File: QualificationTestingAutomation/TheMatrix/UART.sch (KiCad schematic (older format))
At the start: 23 parts, among them Q3 2N7002DW, Q4 2N7002DW, Q5 2N7002DW, Q6 2N7002DW, U20 CD4070B, U32 MAX324CUA

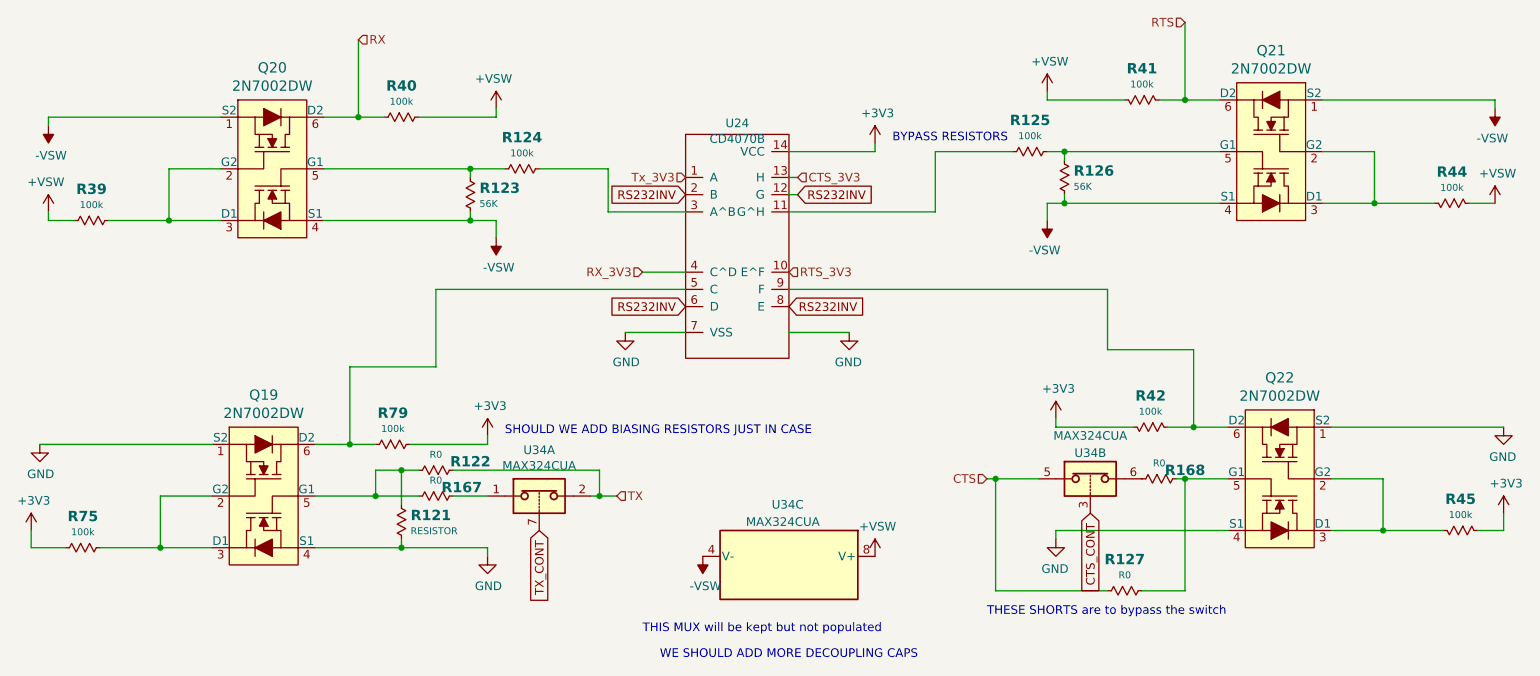
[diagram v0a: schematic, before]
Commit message: Added 60V supply for the MUX's so they can be independent from Vpower, Added another seperate power rail
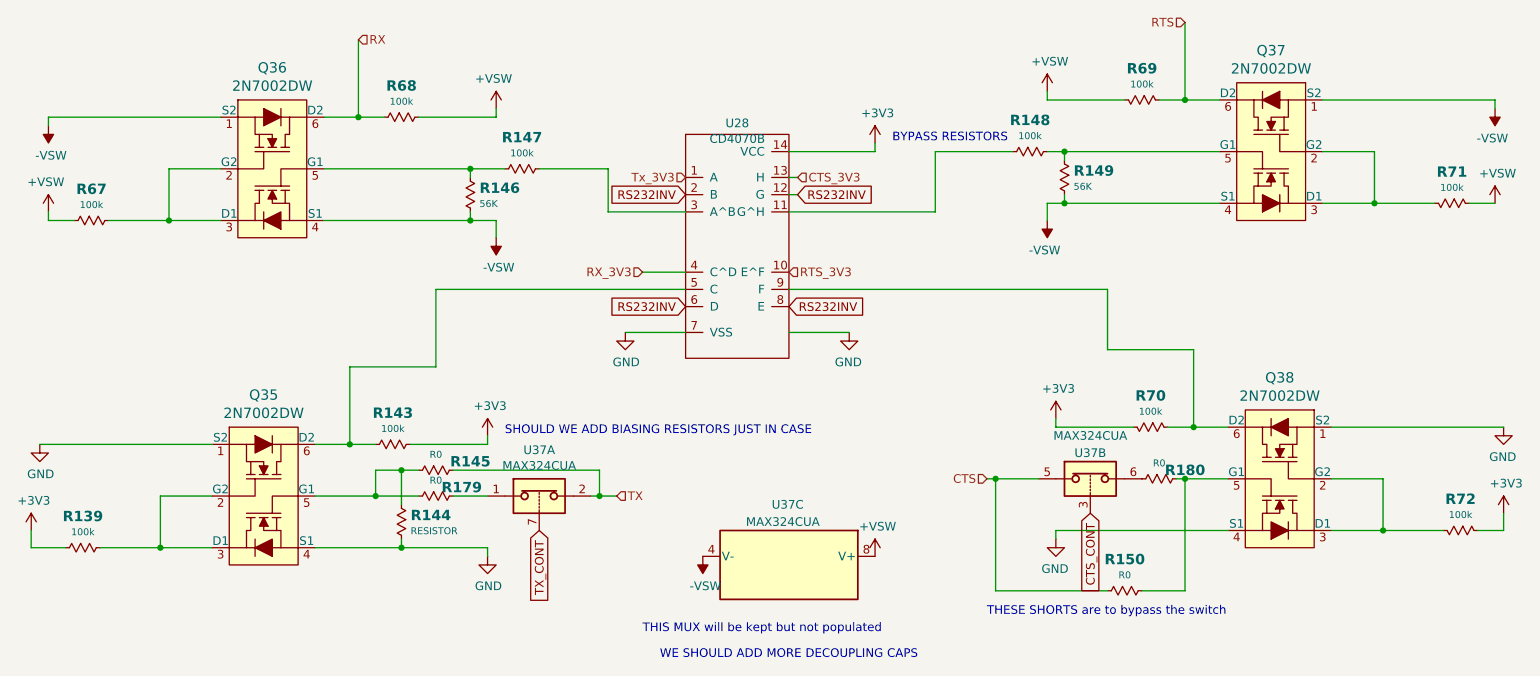
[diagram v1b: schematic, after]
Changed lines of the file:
@@
 AR Path="/5BB9E3C7/5BDC515F/5C46C762" Ref="Q35"  Part="1"
 AR Path="/5BB9E3C7/5BDC5169/5C46C762" Ref="Q39"  Part="1"
-F 0 "Q19" H 3450 4987 60  0000 C CNN
+F 0 "Q35" H 3450 4987 60  0000 C CNN
 F 1 "2N7002DW" H 3450 4881 60  0000 C CNN
 F 2 "digikey-footprints:SOT-363" H 3650 4700 60  0001 L CNN
@@
 AR Path="/5BB9E3C7/5BDC515F/5C46C76E" Ref="R143"  Part="1"
 AR Path="/5BB9E3C7/5BDC5169/5C46C76E" Ref="R159"  Part="1"
-F 0 "R79" H 4200 4482 60  0000 C CNB
+F 0 "R143" H 4200 4482 60  0000 C CNB
 F 1 "100k" H 4200 4391 40  0000 C CNN
 F 2 "Resistor_SMD:R_0402_1005Metric" H 4200 4160 40  0001 C CNN
@@
 AR Path="/5BB9E3C7/5BDC515F/5C46C789" Ref="R139"  Part="1"
 AR Path="/5BB9E3C7/5BDC5169/5C46C789" Ref="R155"  Part="1"
-F 0 "R75" H 2400 5082 60  0000 C CNB
+F 0 "R139" H 2400 5082 60  0000 C CNB
 F 1 "100k" H 2400 4991 40  0000 C CNN
 F 2 "Resistor_SMD:R_0402_1005Metric" H 2400 4760 40  0001 C CNN
@@
 AR Path="/5BB9E3C7/5BDC515F/5BC01C7A" Ref="Q36"  Part="1"
 AR Path="/5BB9E3C7/5BDC5169/5BC01C7A" Ref="Q40"  Part="1"
-F 0 "Q20" H 3500 3087 60  0000 C CNN
+F 0 "Q36" H 3500 3087 60  0000 C CNN
 F 1 "2N7002DW" H 3500 2981 60  0000 C CNN
 F 2 "digikey-footprints:SOT-363" H 3700 2800 60  0001 L CNN
@@
 AR Path="/5BB9E3C7/5BDC515F/5BC01C85" Ref="R68"  Part="1"
 AR Path="/5BB9E3C7/5BDC5169/5BC01C85" Ref="R74"  Part="1"
-F 0 "R40" H 4250 2582 60  0000 C CNB
+F 0 "R68" H 4250 2582 60  0000 C CNB
 F 1 "100k" H 4250 2491 40  0000 C CNN
 F 2 "Resistor_SMD:R_0402_1005Metric" H 4250 2260 40  0001 C CNN
@@
 AR Path="/5BB9E3C7/5BDC515F/5BC01C95" Ref="R67"  Part="1"
 AR Path="/5BB9E3C7/5BDC5169/5BC01C95" Ref="R73"  Part="1"
-F 0 "R39" H 2450 3182 60  0000 C CNB
+F 0 "R67" H 2450 3182 60  0000 C CNB
 F 1 "100k" H 2450 3091 40  0000 C CNN
 F 2 "Resistor_SMD:R_0402_1005Metric" H 2450 2860 40  0001 C CNN
@@
 AR Path="/5BB9E3C7/5BDC515F/5BC141FA" Ref="Q38"  Part="1"
 AR Path="/5BB9E3C7/5BDC5169/5BC141FA" Ref="Q42"  Part="1"
-F 0 "Q22" H 9350 4887 60  0000 C CNN
+F 0 "Q38" H 9350 4887 60  0000 C CNN
 F 1 "2N7002DW" H 9350 4781 60  0000 C CNN
 F 2 "digikey-footprints:SOT-363" H 9550 4600 60  0001 L CNN
@@
 AR Path="/5BB9E3C7/5BDC515F/5BC14205" Ref="R70"  Part="1"
 AR Path="/5BB9E3C7/5BDC5169/5BC14205" Ref="R77"  Part="1"
-F 0 "R42" H 8600 4382 60  0000 C CNB
+F 0 "R70" H 8600 4382 60  0000 C CNB
 F 1 "100k" H 8600 4291 40  0000 C CNN
 F 2 "Resistor_SMD:R_0402_1005Metric" H 8600 4060 40  0001 C CNN
@@
 AR Path="/5BB9E3C7/5BDC515F/5BC14215" Ref="R72"  Part="1"
 AR Path="/5BB9E3C7/5BDC5169/5BC14215" Ref="R80"  Part="1"
-F 0 "R45" H 10400 4982 60  0000 C CNB
+F 0 "R72" H 10400 4982 60  0000 C CNB
 F 1 "100k" H 10400 4891 40  0000 C CNN
 F 2 "Resistor_SMD:R_0402_1005Metric" H 10400 4660 40  0001 C CNN
@@
 AR Path="/5BB9E3C7/5BDC515F/5BC14248" Ref="Q37"  Part="1"
 AR Path="/5BB9E3C7/5BDC5169/5BC14248" Ref="Q41"  Part="1"
-F 0 "Q21" H 9300 2987 60  0000 C CNN
+F 0 "Q37" H 9300 2987 60  0000 C CNN
 F 1 "2N7002DW" H 9300 2881 60  0000 C CNN
 F 2 "digikey-footprints:SOT-363" H 9500 2700 60  0001 L CNN
@@
 AR Path="/5BB9E3C7/5BDC515F/5BC14252" Ref="R69"  Part="1"
 AR Path="/5BB9E3C7/5BDC5169/5BC14252" Ref="R76"  Part="1"
-F 0 "R41" H 8550 2482 60  0000 C CNB
+F 0 "R69" H 8550 2482 60  0000 C CNB
 F 1 "100k" H 8550 2391 40  0000 C CNN
 F 2 "Resistor_SMD:R_0402_1005Metric" H 8550 2160 40  0001 C CNN
@@
 AR Path="/5BB9E3C7/5BDC515F/5BC14262" Ref="R71"  Part="1"
 AR Path="/5BB9E3C7/5BDC5169/5BC14262" Ref="R78"  Part="1"
-F 0 "R44" H 10350 3082 60  0000 C CNB
+F 0 "R71" H 10350 3082 60  0000 C CNB
 F 1 "100k" H 10350 2991 40  0000 C CNN
 F 2 "Resistor_SMD:R_0402_1005Metric" H 10350 2760 40  0001 C CNN
@@
 AR Path="/5BB9E3C7/5BD54793/5BD62A8F" Ref="U36"  Part="1"
 AR Path="/5BB9E3C7/5BDC515F/5BD62A8F" Ref="U37"  Part="1"
-F 0 "U34" H 5050 4867 50  0000 C CNN
+F 0 "U37" H 5050 4867 50  0000 C CNN
 F 1 "MAX324CUA" H 5050 4776 50  0000 C CNN
 F 2 "Housings_SSOP:MSOP-8_3x3mm_Pitch0.65mm" H 5050 4500 50  0001 C CNN
@@
 AR Path="/5BB9E3C7/5BD54793/5BD6777D" Ref="U36"  Part="2"
 AR Path="/5BB9E3C7/5BDC515F/5BD6777D" Ref="U37"  Part="2"
-F 0 "U34" H 8250 4650 50  0000 C CNN
+F 0 "U37" H 8250 4650 50  0000 C CNN
 F 1 "MAX324CUA" H 8250 4750 50  0000 C CNN
 F 2 "Housings_SSOP:MSOP-8_3x3mm_Pitch0.65mm" H 8250 4400 50  0001 C CNN
@@
 AR Path="/5BB9E3C7/5BD54793/5BD79DC1" Ref="U36"  Part="3"
 AR Path="/5BB9E3C7/5BDC515F/5BD79DC1" Ref="U37"  Part="3"
-F 0 "U34" V 6200 4850 50  0000 L CNN
+F 0 "U37" V 6200 4850 50  0000 L CNN
 F 1 "MAX324CUA" V 6300 4700 50  0000 L CNN
 F 2 "Housings_SSOP:MSOP-8_3x3mm_Pitch0.65mm" H 6500 4850 50  0001 C CNN
@@
 AR Path="/5BB9E3C7/5BD54793/5BBE173B" Ref="R136"  Part="1"
 AR Path="/5BB9E3C7/5BDC515F/5BBE173B" Ref="R145"  Part="1"
-F 0 "R122" H 4650 4500 60  0000 C CNB
+F 0 "R145" H 4650 4500 60  0000 C CNB
 F 1 "R0" H 4450 4541 40  0000 C CNN
 F 2 "Resistor_SMD:R_0402_1005Metric" H 4450 4310 40  0001 C CNN
@@
 AR Path="/5BB9E3C7/5BD54793/5BBEA4F3" Ref="R142"  Part="1"
 AR Path="/5BB9E3C7/5BDC515F/5BBEA4F3" Ref="R150"  Part="1"
-F 0 "R127" H 8450 5332 60  0000 C CNB
+F 0 "R150" H 8450 5332 60  0000 C CNB
 F 1 "R0" H 8450 5241 40  0000 C CNN
 F 2 "Resistor_SMD:R_0402_1005Metric" H 8450 5010 40  0001 C CNN
@@
 AR Path="/5BB9E3C7/5BDC515F/5BBECE3B" Ref="R147"  Part="1"
 AR Path="/5BB9E3C7/5BDC5169/5BBECE3B" Ref="R?"  Part="1"
-F 0 "R124" H 4950 2882 60  0000 C CNB
+F 0 "R147" H 4950 2882 60  0000 C CNB
 F 1 "100k" H 4950 2791 40  0000 C CNN
 F 2 "Resistor_SMD:R_0402_1005Metric" H 4950 2560 40  0001 C CNN
@@
 AR Path="/5BB9E3C7/5BD54793/5BBF422E" Ref="R137"  Part="1"
 AR Path="/5BB9E3C7/5BDC515F/5BBF422E" Ref="R146"  Part="1"
-F 0 "R123" V 4612 2903 60  0000 L CNB
+F 0 "R146" V 4612 2903 60  0000 L CNB
 F 1 "56K" V 4703 2903 40  0000 L CNN
 F 2 "Resistor_SMD:R_0402_1005Metric" H 4650 2710 40  0001 C CNN
@@
 AR Path="/5BB9E3C7/5BDC515F/5BBF9882" Ref="R148"  Part="1"
 AR Path="/5BB9E3C7/5BDC5169/5BBF9882" Ref="R?"  Part="1"
-F 0 "R125" H 7900 2782 60  0000 C CNB
+F 0 "R148" H 7900 2782 60  0000 C CNB
 F 1 "100k" H 7900 2691 40  0000 C CNN
 F 2 "Resistor_SMD:R_0402_1005Metric" H 7900 2460 40  0001 C CNN
@@
 AR Path="/5BB9E3C7/5BD54793/5BC047FB" Ref="R141"  Part="1"
 AR Path="/5BB9E3C7/5BDC515F/5BC047FB" Ref="R149"  Part="1"
-F 0 "R126" V 8062 2803 60  0000 L CNB
+F 0 "R149" V 8062 2803 60  0000 L CNB
 F 1 "56K" V 8153 2803 40  0000 L CNN
 F 2 "Resistor_SMD:R_0402_1005Metric" H 8100 2610 40  0001 C CNN
@@
 AR Path="/5BB9E3C7/5BD54793/5BC0A9BF" Ref="R135"  Part="1"
 AR Path="/5BB9E3C7/5BDC515F/5BC0A9BF" Ref="R144"  Part="1"
-F 0 "R121" V 4212 4803 60  0000 L CNB
+F 0 "R144" V 4212 4803 60  0000 L CNB
 F 1 "RESISTOR" V 4303 4803 40  0000 L CNN
 F 2 "Resistor_SMD:R_0402_1005Metric" H 4250 4610 40  0001 C CNN
@@
 AR Path="/5BB9E3C7/5BDC5169/5C46C7B8" Ref="U29"  Part="1"
 AR Path="/5C46C7B8" Ref="U24"  Part="1"
-F 0 "U24" H 6200 2365 50  0000 C CNN
+F 0 "U28" H 6200 2365 50  0000 C CNN
 F 1 "CD4070B" H 6200 2274 50  0000 C CNN
 F 2 "digikey-footprints:SOIC-14_W3.9mm" H 6150 2350 50  0001 C CNN
@@
 AR Path="/5BB9E3C7/5BD54793/5CACEC46" Ref="R177"  Part="1"
 AR Path="/5BB9E3C7/5BDC515F/5CACEC46" Ref="R179"  Part="1"
-F 0 "R167" H 4600 4650 60  0000 C CNB
+F 0 "R179" H 4600 4650 60  0000 C CNB
 F 1 "R0" H 4450 4691 40  0000 C CNN
 F 2 "Resistor_SMD:R_0402_1005Metric" H 4450 4460 40  0001 C CNN
@@
 AR Path="/5BB9E3C7/5BD54793/5CAD91E6" Ref="R178"  Part="1"
 AR Path="/5BB9E3C7/5BDC515F/5CAD91E6" Ref="R180"  Part="1"
-F 0 "R168" H 8800 4550 60  0000 C CNB
+F 0 "R180" H 8800 4550 60  0000 C CNB
 F 1 "R0" H 8650 4591 40  0000 C CNN
 F 2 "Resistor_SMD:R_0402_1005Metric" H 8650 4360 40  0001 C CNN

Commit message: Major upgrade, Finished laying out switcheroo, and the Matrix.
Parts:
- U11: renamed from U32; footprint Housings_SSOP:MSOP-8_3x3mm_Pitch0.65mm -> Package_SO:MSOP-8_3x3mm_P0.65mm
- U12: renamed from U20; Preferable Alternative (none) -> SN74LVC86ADR
- renumbered Q3 to Q2, Q4 to Q3, Q5 to Q4, Q6 to Q5, R15 to R10, R13 to R11, R105 to R12, R106 to R21, R163 to R42, R108 to R43, R93 to R44, R94 to R45, R112 to R46, R113 to R47, R14 to R48, R16 to R49, R164 to R51, R17 to R52, R18 to R53, R11 to R8, R12 to R9
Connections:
- net +VSW: now also U11.8 (V+); no longer U11.8 (V+)
- net -VSW: now also U11.4 (V-); no longer U11.4 (V-)
- net CTS: now also U11.5; no longer U11.5
- net CTS_CONT: now also U11.3; no longer U11.3
- net at R51.1: now also U11.6; no longer U11.6
